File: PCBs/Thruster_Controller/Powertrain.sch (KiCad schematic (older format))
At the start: 54 parts, among them Q1 SIZF906DT, Q2 SIZF906DT, Q3 SIZF906DT, U1 DRV8305

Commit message: BOM Changes
- Found cheaper alternatives for some components
- Changed sizing of some components to reduce cost where possible
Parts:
- R10: footprint Resistors_SMD:R_0603 -> Resistors_SMD:R_0805; Digikey RHM330DCT-ND -> 2019-RK73B2ATTD331JCT-ND
- R11, R8, R9: footprint MCU_Powertrain:R_2512_Sense -> Resistors_SMD:R_2512; Digikey YAG6124CT-ND -> YAG6105CT-ND
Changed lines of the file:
@@
 F 0 "R10" H 1018 2471 50  0000 L CNN
 F 1 "330" H 1018 2380 50  0000 L CNN
-F 2 "Resistors_SMD:R_0603" V 990 2415 50  0001 C CNN
+F 2 "Resistors_SMD:R_0805" V 990 2415 50  0001 C CNN
 F 3 "~" H 950 2425 50  0001 C CNN
-F 4 "RHM330DCT-ND" H 950 2425 50  0001 C CNN "Digikey"
+F 4 "2019-RK73B2ATTD331JCT-ND" H 950 2425 50  0001 C CNN "Digikey"
 	1    950  2425
 	1    0    0    -1
@@
 F 0 "R11" H 6168 2471 50  0000 L CNN
 F 1 "5m" H 6168 2380 50  0000 L CNN
-F 2 "MCU_Powertrain:R_2512_Sense" V 6140 2415 50  0001 C CNN
+F 2 "Resistors_SMD:R_2512" V 6140 2415 50  0001 C CNN
 F 3 "" H 6100 2425 50  0001 C CNN
-F 4 "YAG6124CT-ND" H 6100 2425 50  0001 C CNN "Digikey"
+F 4 "YAG6105CT-ND" H 6100 2425 50  0001 C CNN "Digikey"
 	1    6100 2425
 	1    0    0    -1
@@
 F 0 "R8" H 8118 2471 50  0000 L CNN
 F 1 "5m" H 8118 2380 50  0000 L CNN
-F 2 "MCU_Powertrain:R_2512_Sense" V 8090 2415 50  0001 C CNN
+F 2 "Resistors_SMD:R_2512" V 8090 2415 50  0001 C CNN
 F 3 "" H 8050 2425 50  0001 C CNN
-F 4 "YAG6124CT-ND" H 8050 2425 50  0001 C CNN "Digikey"
+F 4 "YAG6105CT-ND" H 8050 2425 50  0001 C CNN "Digikey"
 	1    8050 2425
 	1    0    0    -1
@@
 F 0 "R9" H 10013 2466 50  0000 L CNN
 F 1 "5m" H 10013 2375 50  0000 L CNN
-F 2 "MCU_Powertrain:R_2512_Sense" V 9985 2410 50  0001 C CNN
+F 2 "Resistors_SMD:R_2512" V 9985 2410 50  0001 C CNN
 F 3 "" H 9945 2420 50  0001 C CNN
-F 4 "YAG6124CT-ND" H 9945 2420 50  0001 C CNN "Digikey"
+F 4 "YAG6105CT-ND" H 9945 2420 50  0001 C CNN "Digikey"
 	1    9945 2420
 	1    0    0    -1

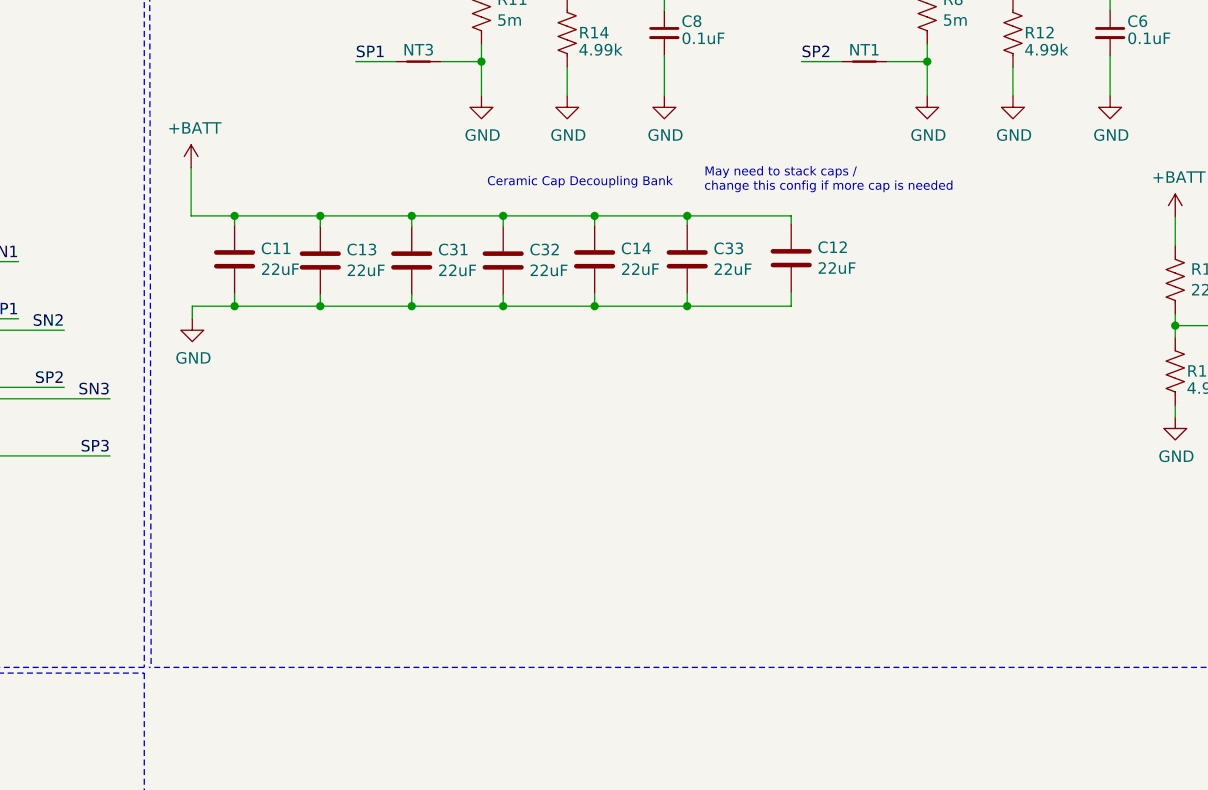
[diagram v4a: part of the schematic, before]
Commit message: Changed Cap Bank + Gerbers
- Changed cap bank to 3 aluminum poly caps plus 3 ceramic caps
- Fixed routing
- Generated Gerbers
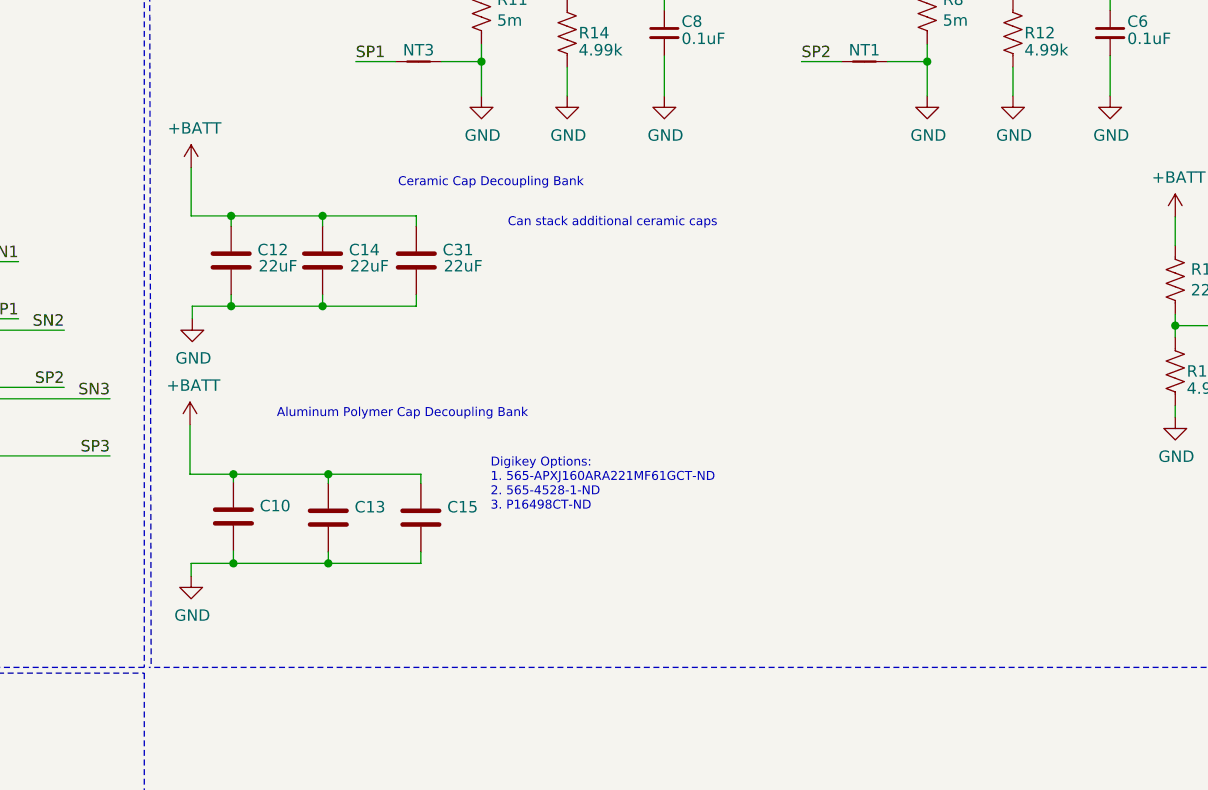
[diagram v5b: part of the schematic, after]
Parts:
- removed C11, C32, C33: 22uF, Capacitors_SMD:C_1812, symbol Device:C
- added C10, C15: 22uF, Capacitors_SMD:CP_Elec_6.3x5.8, symbol Device:C
- C12, C14, C31: footprint Capacitors_SMD:C_1812 -> Capacitors_SMD:C_1206; Digikey 445-1607-1-ND -> 1276-1101-1-ND
- C13: footprint Capacitors_SMD:C_1812 -> Capacitors_SMD:CP_Elec_6.3x5.8; Digikey 445-1607-1-ND -> 565-APXJ160ARA221MF61GCT-ND
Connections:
- net +BATT: now also C10.1, C15.1
- net GND: now also C10.2, C15.2
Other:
- note added: "Aluminum Polymer Cap Decoupling Bank"
- note added: "Can stack additional ceramic caps"
- note added: "Digikey Options:\n1. 565-APXJ160ARA221MF61GCT-ND\n2. 565-4528-1-ND\n3. P16498CT-ND"
- note removed: "May need to stack caps / \nchange this config if more cap is needed"
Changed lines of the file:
@@
 Text Label 9960 3805 2    50   ~ 0
 VSEN_PVDD
-Text Notes 6125 3205 0    39   ~ 0
+Text Notes 5735 3205 0    39   ~ 0
 Ceramic Cap Decoupling Bank
 $Comp
@@
 Wire Wire Line
 	9135 3330 9135 3455
-$Comp
-L Device:C C31
-U 1 1 5E94AEE5
-P 5795 3520
-F 0 "C31" H 5910 3566 50  0000 L CNN
-F 1 "22uF" H 5910 3475 50  0000 L CNN
-F 2 "Capacitors_SMD:C_1812" H 5833 3370 50  0001 C CNN
-F 3 "~" H 5795 3520 50  0001 C CNN
-F 4 "445-1607-1-ND" H 5795 3520 50  0001 C CNN "Digikey"
-	1    5795 3520
-	1    0    0    -1
-$EndComp
-$Comp
-L Device:C C13
-U 1 1 5E9994E5
-P 5395 3520
-F 0 "C13" H 5510 3566 50  0000 L CNN
-F 1 "22uF" H 5510 3475 50  0000 L CNN
-F 2 "Capacitors_SMD:C_1812" H 5433 3370 50  0001 C CNN
-F 3 "~" H 5395 3520 50  0001 C CNN
-F 4 "445-1607-1-ND" H 5395 3520 50  0001 C CNN "Digikey"
-	1    5395 3520
-	1    0    0    -1
-$EndComp
-$Comp
-L Device:C C11
-U 1 1 5E99C3C9
-P 5020 3515
-F 0 "C11" H 5135 3561 50  0000 L CNN
-F 1 "22uF" H 5135 3470 50  0000 L CNN
-F 2 "Capacitors_SMD:C_1812" H 5058 3365 50  0001 C CNN
-F 3 "~" H 5020 3515 50  0001 C CNN
-F 4 "445-1607-1-ND" H 5020 3515 50  0001 C CNN "Digikey"
-	1    5020 3515
-	1    0    0    -1
-$EndComp
-$Comp
-L Device:C C32
-U 1 1 5EB6ADB0
-P 6195 3520
-F 0 "C32" H 6310 3566 50  0000 L CNN
-F 1 "22uF" H 6310 3475 50  0000 L CNN
-F 2 "Capacitors_SMD:C_1812" H 6233 3370 50  0001 C CNN
-F 3 "~" H 6195 3520 50  0001 C CNN
-F 4 "445-1607-1-ND" H 6195 3520 50  0001 C CNN "Digikey"
-	1    6195 3520
-	1    0    0    -1
-$EndComp
-$Comp
-L Device:C C12
-U 1 1 5EBA4513
-P 7455 3510
-F 0 "C12" H 7570 3556 50  0000 L CNN
-F 1 "22uF" H 7570 3465 50  0000 L CNN
-F 2 "Capacitors_SMD:C_1812" H 7493 3360 50  0001 C CNN
-F 3 "~" H 7455 3510 50  0001 C CNN
-F 4 "445-1607-1-ND" H 7455 3510 50  0001 C CNN "Digikey"
-	1    7455 3510
-	1    0    0    -1
-$EndComp
-$Comp
-L Device:C C33
-U 1 1 5EBA4521
-P 7000 3515
-F 0 "C33" H 7115 3561 50  0000 L CNN
-F 1 "22uF" H 7115 3470 50  0000 L CNN
-F 2 "Capacitors_SMD:C_1812" H 7038 3365 50  0001 C CNN
-F 3 "~" H 7000 3515 50  0001 C CNN
-F 4 "445-1607-1-ND" H 7000 3515 50  0001 C CNN "Digikey"
-	1    7000 3515
-	1    0    0    -1
-$EndComp
 Wire Wire Line
 	4830 3115 4830 3325
 Wire Wire Line
-	5395 3325 5395 3370
-Wire Wire Line
-	5395 3325 5795 3325
-Wire Wire Line
-	5795 3325 5795 3370
-Connection ~ 5395 3325
-Wire Wire Line
-	5795 3325 6195 3325
-Connection ~ 5795 3325
-Wire Wire Line
-	6195 3325 6595 3325
-Wire Wire Line
-	6595 3325 6595 3365
-Connection ~ 6195 3325
+	5005 3325 5005 3370
+Wire Wire Line
+	5005 3325 5405 3325
+Connection ~ 5005 3325
 $Comp
 L power:GND #PWR0106
@@
 $EndComp
 Wire Wire Line
-	5395 3720 5395 3670
-Wire Wire Line
-	5395 3720 5795 3720
-Wire Wire Line
-	5795 3720 5795 3670
-Wire Wire Line
-	6195 3720 6195 3670
-Connection ~ 5795 3720
-Wire Wire Line
-	5795 3720 6195 3720
-Connection ~ 6195 3720
-Wire Wire Line
-	6195 3720 6595 3720
-Wire Wire Line
-	6595 3665 6595 3720
-Connection ~ 6595 3720
-Text Notes 7075 3225 0    39   ~ 0
-May need to stack caps / \nchange this config if more cap is needed
-Wire Wire Line
-	4830 3325 5020 3325
-Wire Wire Line
-	6195 3325 6195 3370
+	5005 3720 5005 3670
+Wire Wire Line
+	5005 3720 5405 3720
+Wire Wire Line
+	4835 3720 4835 3775
+Connection ~ 5005 3720
+Text Notes 5205 4215 0    39   ~ 0
+Aluminum Polymer Cap Decoupling Bank
+$Comp
+L power:+BATT #PWR0156
+U 1 1 5E8C169E
+P 4825 4240
+F 0 "#PWR0156" H 4825 4090 50  0001 C CNN
+F 1 "+BATT" H 4840 4413 50  0000 C CNN
+F 2 "" H 4825 4240 50  0001 C CNN
+F 3 "" H 4825 4240 50  0001 C CNN
+	1    4825 4240
+	1    0    0    -1
+$EndComp
+$Comp
+L Device:C C15
+U 1 1 5E8C16A5
+P 5835 4645
+F 0 "C15" H 5950 4691 50  0000 L CNN
+F 1 "22uF" H 5950 4600 50  0001 L CNN
+F 2 "Capacitors_SMD:CP_Elec_6.3x5.8" H 5873 4495 50  0001 C CNN
+F 3 "~" H 5835 4645 50  0001 C CNN
+F 4 "565-APXJ160ARA221MF61GCT-ND" H 5835 4645 50  0001 C CNN "Digikey"
+	1    5835 4645
+	1    0    0    -1
+$EndComp
+$Comp
+L Device:C C13
+U 1 1 5E8C16AC
+P 5430 4645
+F 0 "C13" H 5545 4691 50  0000 L CNN
+F 1 "22uF" H 5545 4600 50  0001 L CNN
+F 2 "Capacitors_SMD:CP_Elec_6.3x5.8" H 5468 4495 50  0001 C CNN
+F 3 "~" H 5430 4645 50  0001 C CNN
+F 4 "565-APXJ160ARA221MF61GCT-ND" H 5430 4645 50  0001 C CNN "Digikey"
+	1    5430 4645
+	1    0    0    -1
+$EndComp
+$Comp
+L Device:C C10
+U 1 1 5E8C16B3
+P 5015 4640
+F 0 "C10" H 5130 4686 50  0000 L CNN
+F 1 "22uF" H 5130 4595 50  0001 L CNN
+F 2 "Capacitors_SMD:CP_Elec_6.3x5.8" H 5053 4490 50  0001 C CNN
+F 3 "~" H 5015 4640 50  0001 C CNN
+F 4 "565-APXJ160ARA221MF61GCT-ND" H 5015 4640 50  0001 C CNN "Digikey"
+	1    5015 4640
+	1    0    0    -1
+$EndComp
+Wire Wire Line
+	4825 4240 4825 4455
+Wire Wire Line
+	5430 4455 5430 4495
+Wire Wire Line
+	5430 4455 5835 4455
+Wire Wire Line
+	5835 4455 5835 4495
+Connection ~ 5430 4455
+$Comp
+L power:GND #PWR0157
+U 1 1 5E8C16D8
+P 4830 4900
+F 0 "#PWR0157" H 4830 4650 50  0001 C CNN
+F 1 "GND" H 4835 4727 50  0000 C CNN
+F 2 "" H 4830 4900 50  0001 C CNN
+F 3 "" H 4830 4900 50  0001 C CNN
+	1    4830 4900
+	1    0    0    -1
+$EndComp
+Wire Wire Line
+	5430 4845 5430 4795
+Wire Wire Line
+	5430 4845 5835 4845
+Wire Wire Line
+	5835 4845 5835 4795
+Wire Wire Line
+	4825 4455 5015 4455
+Wire Wire Line
+	5015 4790 5015 4845
+Wire Wire Line
+	5015 4845 4830 4845
+Wire Wire Line
+	4830 4845 4830 4900
+Wire Wire Line
+	5015 4455 5015 4490
+Connection ~ 5015 4455
+Wire Wire Line
+	5015 4455 5430 4455
+Wire Wire Line
+	5015 4845 5430 4845
+Connection ~ 5015 4845
+Connection ~ 5430 4845
+Text Notes 6140 4620 0    39   ~ 0
+Digikey Options:\n1. 565-APXJ160ARA221MF61GCT-ND\n2. 565-4528-1-ND\n3. P16498CT-ND
+$Comp
+L Device:C C12
+U 1 1 5EA29A4D
+P 5005 3520
+F 0 "C12" H 5120 3566 50  0000 L CNN
+F 1 "22uF" H 5125 3495 50  0000 L CNN
+F 2 "Capacitors_SMD:C_1206" H 5043 3370 50  0001 C CNN
+F 3 "~" H 5005 3520 50  0001 C CNN
+F 4 "1276-1101-1-ND" H 5005 3520 50  0001 C CNN "Digikey"
+	1    5005 3520
+	1    0    0    -1
+$EndComp
+Wire Wire Line
+	5405 3720 5405 3670
+Wire Wire Line
+	5405 3325 5405 3370
 $Comp
 L Device:C C14
-U 1 1 5E9E9892
-P 6595 3515
-F 0 "C14" H 6710 3561 50  0000 L CNN
-F 1 "22uF" H 6710 3470 50  0000 L CNN
-F 2 "Capacitors_SMD:C_1812" H 6633 3365 50  0001 C CNN
-F 3 "~" H 6595 3515 50  0001 C CNN
-F 4 "445-1607-1-ND" H 6595 3515 50  0001 C CNN "Digikey"
-	1    6595 3515
-	1    0    0    -1
-$EndComp
-Wire Wire Line
-	5020 3665 5020 3720
-Wire Wire Line
-	5020 3720 4835 3720
-Wire Wire Line
-	4835 3720 4835 3775
-Wire Wire Line
-	5020 3325 5020 3365
-Connection ~ 5020 3325
-Wire Wire Line
-	5020 3325 5395 3325
-Wire Wire Line
-	5020 3720 5395 3720
-Connection ~ 5020 3720
-Connection ~ 5395 3720
-Wire Wire Line
-	7000 3720 7000 3665
-Wire Wire Line
-	6595 3720 7000 3720
-Wire Wire Line
-	7000 3720 7455 3720
-Wire Wire Line
-	7455 3720 7455 3660
-Connection ~ 7000 3720
-Wire Wire Line
-	7000 3365 7000 3325
-Wire Wire Line
-	7000 3325 6595 3325
-Connection ~ 6595 3325
-Wire Wire Line
-	7455 3325 7000 3325
-Wire Wire Line
-	7455 3325 7455 3360
-Connection ~ 7000 3325
+U 1 1 5EA2C1A5
+P 5405 3520
+F 0 "C14" H 5520 3566 50  0000 L CNN
+F 1 "22uF" H 5525 3495 50  0000 L CNN
+F 2 "Capacitors_SMD:C_1206" H 5443 3370 50  0001 C CNN
+F 3 "~" H 5405 3520 50  0001 C CNN
+F 4 "1276-1101-1-ND" H 5405 3520 50  0001 C CNN "Digikey"
+	1    5405 3520
+	1    0    0    -1
+$EndComp
+$Comp
+L Device:C C31
+U 1 1 5EA2CB0C
+P 5815 3520
+F 0 "C31" H 5930 3566 50  0000 L CNN
+F 1 "22uF" H 5935 3495 50  0000 L CNN
+F 2 "Capacitors_SMD:C_1206" H 5853 3370 50  0001 C CNN
+F 3 "~" H 5815 3520 50  0001 C CNN
+F 4 "1276-1101-1-ND" H 5815 3520 50  0001 C CNN "Digikey"
+	1    5815 3520
+	1    0    0    -1
+$EndComp
+Wire Wire Line
+	5815 3370 5815 3325
+Wire Wire Line
+	5815 3325 5405 3325
+Connection ~ 5405 3325
+Wire Wire Line
+	5815 3670 5815 3720
+Wire Wire Line
+	5815 3720 5405 3720
+Connection ~ 5405 3720
+Wire Wire Line
+	4830 3325 5005 3325
+Wire Wire Line
+	4835 3720 5005 3720
+Text Notes 6215 3380 0    39   ~ 0
+Can stack additional ceramic caps
 $EndSCHEMATC
